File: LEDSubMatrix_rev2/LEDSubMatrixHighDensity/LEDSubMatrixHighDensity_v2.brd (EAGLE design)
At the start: 16.9 x 146 mm, 154 parts, among them IC1 TLC5955DCAR, IC10 SN74LVC1G34DBVR, IC11 SN74LVC1G34DBVR, IC2 TLC5955DCAR, IC3 TLC5955DCAR, IC4 TLC5955DCAR, IC5 TLC5955DCAR, IC6 TLC5955DCAR, IC7 TLC5955DCAR, IC8 TLC5955DCAR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

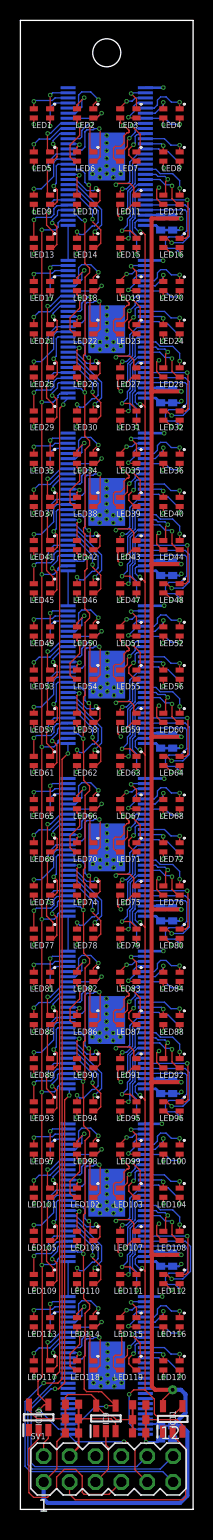
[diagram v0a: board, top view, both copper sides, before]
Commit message: fixed soldermask on led submatrix
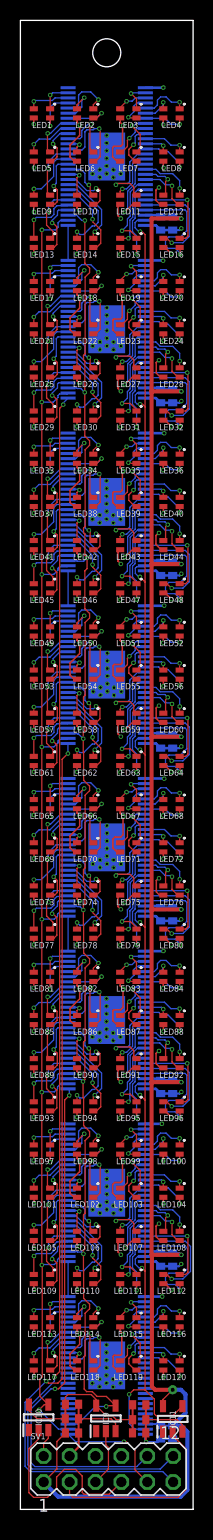
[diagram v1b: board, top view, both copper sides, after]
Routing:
- net 3V3: track 167.5 -> 165.4 mm
- net 3V3_LOGIC: track 221.3 -> 219.5 mm
- net GSCLK_FPGA: track 19.8 -> 19.2 mm
